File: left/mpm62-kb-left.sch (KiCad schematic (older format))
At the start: 59 parts

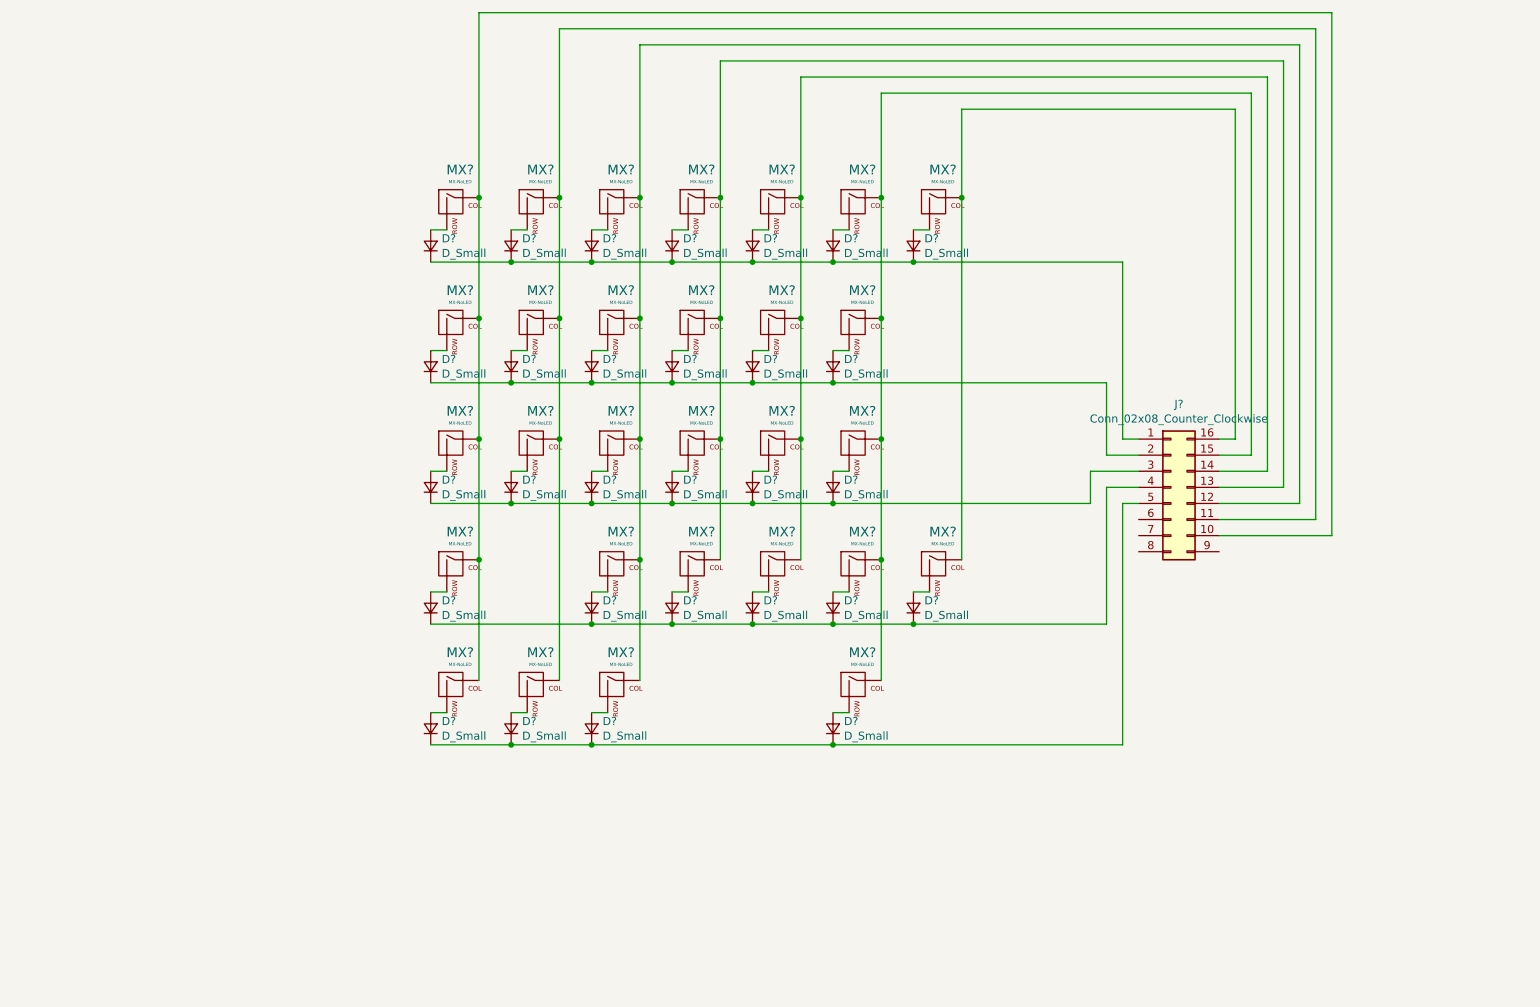
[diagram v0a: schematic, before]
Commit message: complete schematics for both left and right
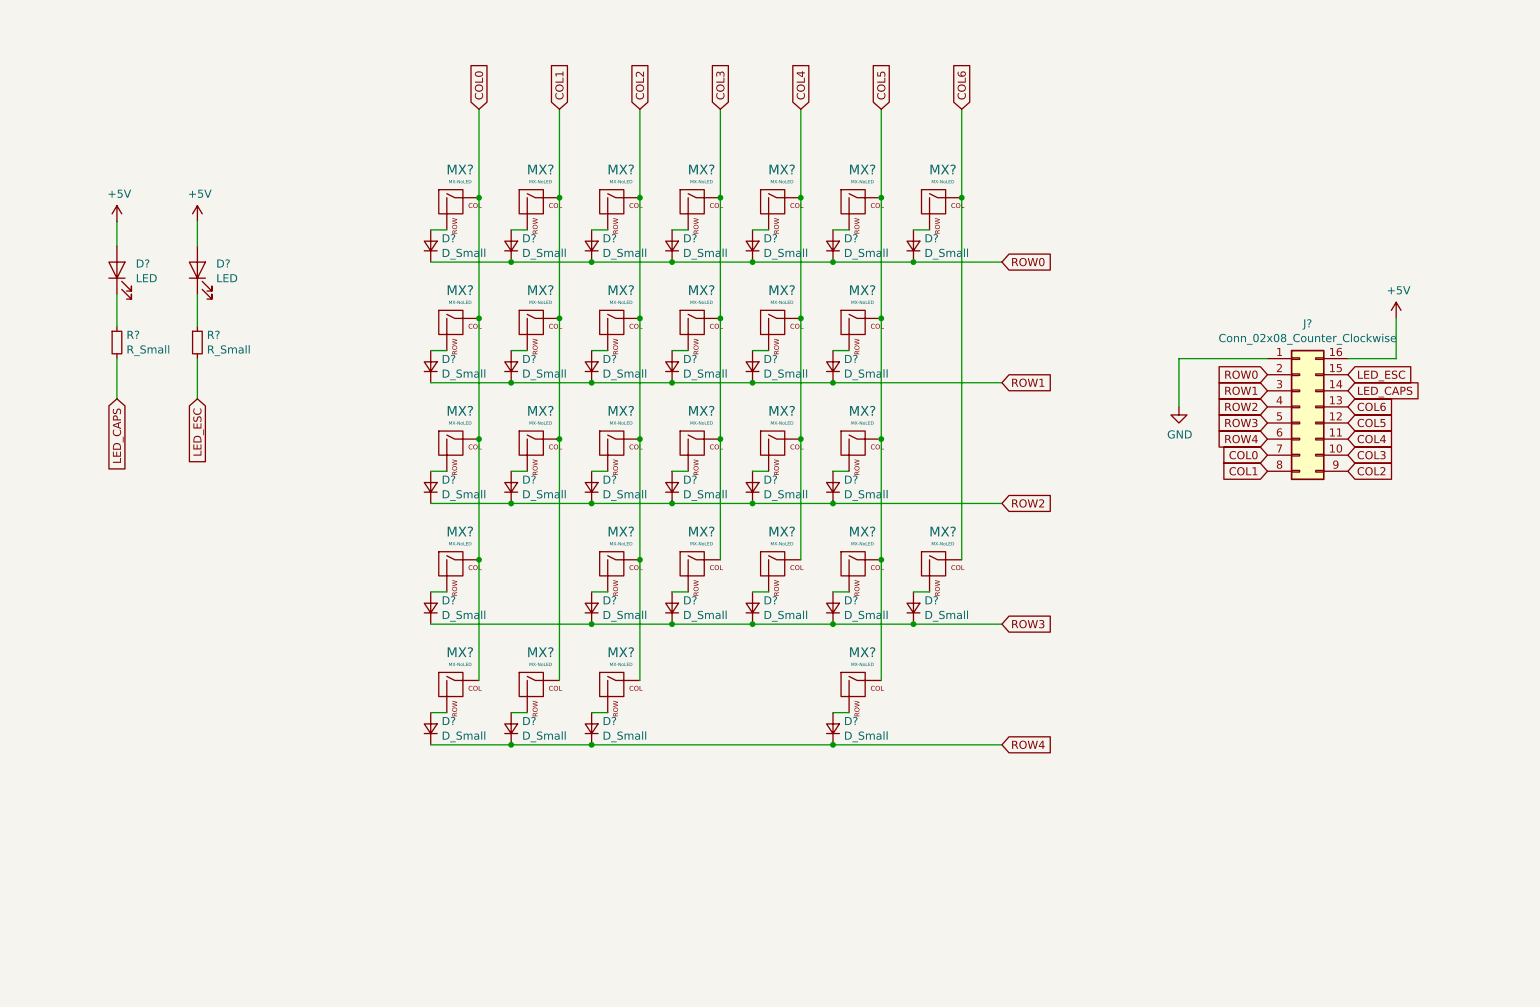
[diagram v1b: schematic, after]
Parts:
- added D? (x2): LED, symbol Device:LED
- added R? (x2): R_Small, symbol Device:R_Small
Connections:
- net COL0: now reaches MX?.1 (COL), MX?.1 (COL), MX?.1 (COL), MX?.1 (COL), MX?.1 (COL)
- net COL0: now also J?.7 (Pin_7); no longer J?.10 (Pin_10)
- net ROW0: now reaches D?.1 (K), D?.1 (K), D?.1 (K), D?.1 (K), D?.1 (K), D?.1 (K), D?.1 (K)
- net ROW0: now also J?.2 (Pin_2); no longer J?.1 (Pin_1)
- net COL1: now reaches MX?.1 (COL), MX?.1 (COL), MX?.1 (COL), MX?.1 (COL)
- net COL1: now also J?.8 (Pin_8); no longer J?.11 (Pin_11)
- net COL2: now reaches MX?.1 (COL), MX?.1 (COL), MX?.1 (COL), MX?.1 (COL), MX?.1 (COL)
- net COL2: now also J?.9 (Pin_9); no longer J?.12 (Pin_12)
- net COL3: now reaches MX?.1 (COL), MX?.1 (COL), MX?.1 (COL), MX?.1 (COL)
- net COL3: now also J?.10 (Pin_10); no longer J?.13 (Pin_13)
- net COL4: now reaches MX?.1 (COL), MX?.1 (COL), MX?.1 (COL), MX?.1 (COL)
- net COL4: now also J?.11 (Pin_11); no longer J?.14 (Pin_14)
- net COL5: now reaches MX?.1 (COL), MX?.1 (COL), MX?.1 (COL), MX?.1 (COL), MX?.1 (COL)
- net COL5: now also J?.12 (Pin_12); no longer J?.15 (Pin_15)
- net COL6: now reaches MX?.1 (COL), MX?.1 (COL)
- net COL6: now also J?.13 (Pin_13); no longer J?.16 (Pin_16)
- net ROW1: now reaches D?.1 (K), D?.1 (K), D?.1 (K), D?.1 (K), D?.1 (K), D?.1 (K)
- net ROW1: now also J?.3 (Pin_3); no longer J?.2 (Pin_2)
- net ROW2: now reaches D?.1 (K), D?.1 (K), D?.1 (K), D?.1 (K), D?.1 (K), D?.1 (K)
- net ROW2: now also J?.4 (Pin_4); no longer J?.3 (Pin_3)
- net ROW3: now reaches D?.1 (K), D?.1 (K), D?.1 (K), D?.1 (K), D?.1 (K), D?.1 (K)
- net ROW3: now also J?.5 (Pin_5); no longer J?.4 (Pin_4)
- net ROW4: now reaches D?.1 (K), D?.1 (K), D?.1 (K), D?.1 (K)
- net ROW4: now also J?.6 (Pin_6); no longer J?.5 (Pin_5)
- new net: D?.1 (K), R?.1 (x2)
- new net +5V: D?.2 (A), D?.2 (A), J?.16 (Pin_16)
- new net GND: J?.1 (Pin_1)
- new net LED_CAPS: J?.14 (Pin_14), R?.2
- new net LED_ESC: J?.15 (Pin_15), R?.2
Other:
- moved on the sheet: J?

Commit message: left side pcb components in place, not routed.
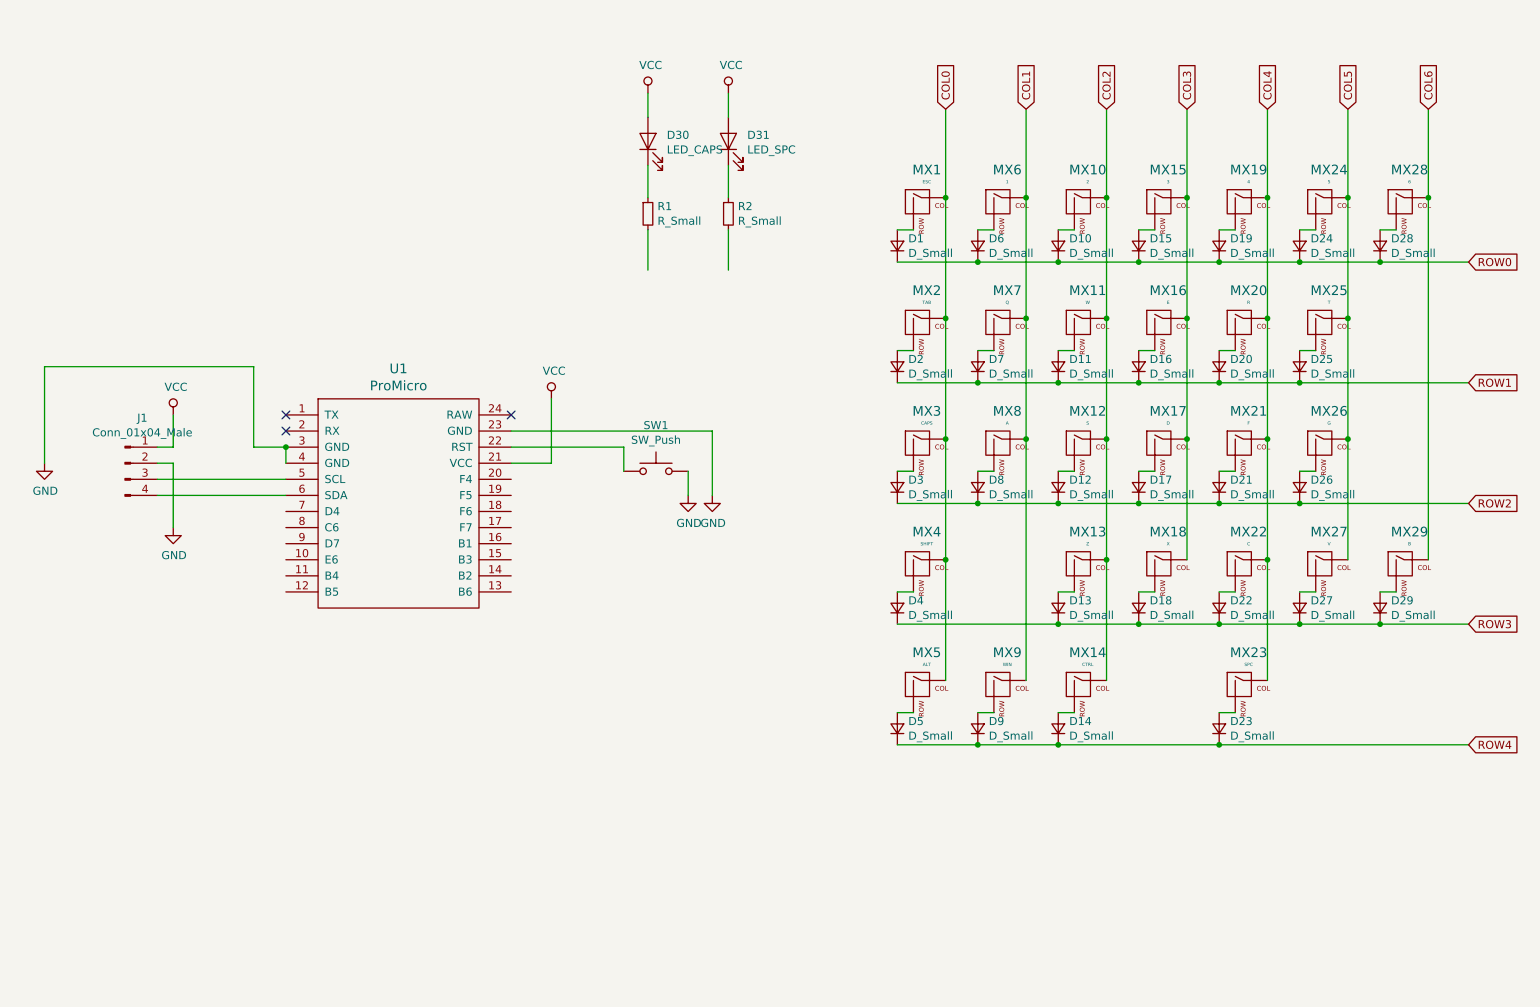
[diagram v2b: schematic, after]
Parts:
- removed J?: Conn_02x08_Counter_Clockwise, symbol Connector_Generic:Conn_02x08_Counter_Clockwise
- added J1: Conn_01x04_Male, Connector_PinHeader_2.54mm:PinHeader_1x04_P2.54mm_Vertical, symbol Connector:Conn_01x04_Male
- added SW1: SW_Push, random-keyboard-parts:SKQG-1155865, symbol Switch:SW_Push
- added U1: ProMicro, promicro:ProMicro, symbol promicro:ProMicro
- D1, D10, D11, D12, D13, D14, D15, D16, D17, D18, D19, D2, D20, D21, D22, D23, D24, D25, D26, D27, D28, D29, D3, D4, D5, D6, D7, D8, D9: renamed from D?; footprint (none) -> Diode_THT:D_DO-35_SOD27_P7.62mm_Horizontal
- D30: renamed from D?; value LED -> LED_CAPS; footprint (none) -> LED_THT:LED_D3.0mm
- D31: renamed from D?; value LED -> LED_SPC; footprint (none) -> LED_THT:LED_D3.0mm
- MX1: renamed from MX?; value MX-NoLED -> ESC; footprint (none) -> MX_Alps_Hybrid:MX-1U-NoLED
- MX10: renamed from MX?; value MX-NoLED -> 2; footprint (none) -> MX_Alps_Hybrid:MX-1U-NoLED
- MX11: renamed from MX?; value MX-NoLED -> W; footprint (none) -> MX_Alps_Hybrid:MX-1U-NoLED
- MX12: renamed from MX?; value MX-NoLED -> S; footprint (none) -> MX_Alps_Hybrid:MX-1U-NoLED
- MX13: renamed from MX?; value MX-NoLED -> Z; footprint (none) -> MX_Alps_Hybrid:MX-1U-NoLED
- MX14: renamed from MX?; value MX-NoLED -> CTRL; footprint (none) -> MX_Alps_Hybrid:MX-1.25U-NoLED
- MX15: renamed from MX?; value MX-NoLED -> 3; footprint (none) -> MX_Alps_Hybrid:MX-1U-NoLED
- MX16: renamed from MX?; value MX-NoLED -> E; footprint (none) -> MX_Alps_Hybrid:MX-1U-NoLED
- MX17: renamed from MX?; value MX-NoLED -> D; footprint (none) -> MX_Alps_Hybrid:MX-1U-NoLED
- MX18: renamed from MX?; value MX-NoLED -> X; footprint (none) -> MX_Alps_Hybrid:MX-1U-NoLED
- MX19: renamed from MX?; value MX-NoLED -> 4; footprint (none) -> MX_Alps_Hybrid:MX-1U-NoLED
- MX2: renamed from MX?; value MX-NoLED -> TAB; footprint (none) -> MX_Alps_Hybrid:MX-1.5U-NoLED
- MX20: renamed from MX?; value MX-NoLED -> R; footprint (none) -> MX_Alps_Hybrid:MX-1U-NoLED
- MX21: renamed from MX?; value MX-NoLED -> F; footprint (none) -> MX_Alps_Hybrid:MX-1U-NoLED
- MX22: renamed from MX?; value MX-NoLED -> C; footprint (none) -> MX_Alps_Hybrid:MX-1U-NoLED
- MX23: renamed from MX?; value MX-NoLED -> SPC; footprint (none) -> MX_Alps_Hybrid:MX-3U-NoLED
- MX24: renamed from MX?; value MX-NoLED -> 5; footprint (none) -> MX_Alps_Hybrid:MX-1U-NoLED
- MX25: renamed from MX?; value MX-NoLED -> T; footprint (none) -> MX_Alps_Hybrid:MX-1U-NoLED
- MX26: renamed from MX?; value MX-NoLED -> G; footprint (none) -> MX_Alps_Hybrid:MX-1U-NoLED
- MX27: renamed from MX?; value MX-NoLED -> V; footprint (none) -> MX_Alps_Hybrid:MX-1U-NoLED
- MX28: renamed from MX?; value MX-NoLED -> 6; footprint (none) -> MX_Alps_Hybrid:MX-1U-NoLED
- MX29: renamed from MX?; value MX-NoLED -> B; footprint (none) -> MX_Alps_Hybrid:MX-1U-NoLED
- MX3: renamed from MX?; value MX-NoLED -> CAPS; footprint (none) -> MX_Alps_Hybrid:MX-1.75U-NoLED
- MX4: renamed from MX?; value MX-NoLED -> SHIFT; footprint (none) -> MX_Alps_Hybrid:MX-2.25U-NoLED
- MX5: renamed from MX?; value MX-NoLED -> ALT; footprint (none) -> MX_Alps_Hybrid:MX-1.25U-NoLED
- MX6: renamed from MX?; value MX-NoLED -> 1; footprint (none) -> MX_Alps_Hybrid:MX-1U-NoLED
- MX7: renamed from MX?; value MX-NoLED -> Q; footprint (none) -> MX_Alps_Hybrid:MX-1U-NoLED
- MX8: renamed from MX?; value MX-NoLED -> A; footprint (none) -> MX_Alps_Hybrid:MX-1U-NoLED
- MX9: renamed from MX?; value MX-NoLED -> WIN; footprint (none) -> MX_Alps_Hybrid:MX-1.25U-NoLED
- R1, R2: renamed from R?; footprint (none) -> Resistor_THT:R_Axial_DIN0204_L3.6mm_D1.6mm_P5.08mm_Horizontal
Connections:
- net COL4: now also MX23.1 (COL)
- net COL5: no longer MX23.1 (COL)
- net GND: now also J1.2 (Pin_2), SW1.2, U1.23 (GND), U1.3 (GND), U1.4 (GND)
- net +5V renamed VCC
- net VCC: now also J1.1 (Pin_1), U1.21 (VCC)
- net LED_CAPS: no longer names the net of R1.2
- net LED_ESC: no longer names the net of R2.2
- new net: SW1.1, U1.22 (RST)
- new net: J1.3 (Pin_3), U1.5 (SCL)
- new net: J1.4 (Pin_4), U1.6 (SDA)
- no-connect marks 0 -> 3
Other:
- moved on the sheet: D1, D10, D11, D12, D13, D14, D15, D16, D17, D18, D19, D2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
